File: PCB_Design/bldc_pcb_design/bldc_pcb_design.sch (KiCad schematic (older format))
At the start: 69 parts, among them IC1 DRV8305NPHPR, J1 Conn_01x04_Female, SW1 BOOT, SW2 RESET, U1 ESP32-WROOM-32D, U10 DS18S20Z+, U2 AS5600-ASOT, U3 LM2672M-3.3, U4 CSD18532NQ5B, U5 CSD18532NQ5B, U6 CSD18532NQ5B, U7 CSD18532NQ5B, U8 CSD18532NQ5B, U9 CSD18532NQ5B

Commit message: Routing Iteration 1 done, Rectified schematics (SOx and shunt resistor connections)
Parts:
- removed C2: 68uF 10V, Capacitor_SMD:C_0603_1608Metric, symbol Device:C
- removed C25, C26, C27: 2.2nF, Capacitor_SMD:C_0603_1608Metric, symbol Device:C
- removed C6: 100uF 100V, Capacitor_SMD:C_0603_1608Metric, symbol Device:C
- added C13, C9: 330uF 50V, Capacitor_SMD:CP_Elec_10x10, symbol Device:CP1
- added C15, C18: 10uF 50V, Capacitor_SMD:C_0603_1608Metric, symbol Device:C
- added C2: 68uF 10V, Capacitor_SMD:CP_Elec_6.3x7.7, symbol Device:CP1
- added C6: 100uF 50V, Capacitor_SMD:CP_Elec_6.3x7.7, symbol Device:CP1
- added H3, H4, H6, H7: MountingHole, MountingHole:MountingHole_4mm, symbol Mechanical:MountingHole
- C24: value 1uF 6.3V -> 1uF 6.3V
- R5: value 10k -> 330
- R6: renamed from R11; footprint (none) -> Shunt_Resistor:Shunt_Resistor_L7.0mm_B4.0mm_H1.0mm
- R7: renamed from R13; footprint (none) -> Shunt_Resistor:Shunt_Resistor_L7.0mm_B4.0mm_H1.0mm
- R8: renamed from R14; footprint (none) -> Shunt_Resistor:Shunt_Resistor_L7.0mm_B4.0mm_H1.0mm
- renumbered C8 to C10, C9 to C11, C16 to C12, C17 to C14, C10 to C16, C11 to C17, C12 to C19, C13 to C20, C14 to C21, C19 to C22, C18 to C23, C20 to C25, C28 to C26, C22 to C27, C29 to C28, C23 to C29, C21 to C30, C15 to C8, D4 to D3, D3 to D4, H4 to H1, H5 to H2, H1 to H5, H2 to H8, H3 to H9, R12 to R10, R6 to R11, R7 to R12, R8 to R13, R9 to R14, R10 to R9
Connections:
- net 3V3_IN: now also C2.1
- net GND: now also R6.2, R7.2, R8.2, C13.2, C15.2, C18.2, C2.2, C6.2, C9.2
- net ISENA: now also IC1.16 (SO1); no longer R6.2
- net ISENB: now also IC1.17 (SO2); no longer R7.2
- net ISENC: now also IC1.18 (SO3); no longer R8.2
- net POWER_IN: now also C13.1, C15.1, C18.1, C6.1, C9.1
- net SLA: now also R6.1
- net SLB: now also R7.1
- net SLC: now also R8.1
- removed net SO1: IC1.16 (SO1), R6.1
- removed net SO2: IC1.17 (SO2), R7.1
- removed net SO3: IC1.18 (SO3), R8.1
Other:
- note added: "Current Amplifier Output Pins going to\nADC Pins of ESP32 Microcontroller"
- note added: "LAYOUT GUIDELINES\n1. PWRGD not connected to MCU** (left NC in REV0)\n2. DVDD and AVDD bypass capacitors close to GND\n3. Flying jump caps close to pins\n4. PVDD cap close to PVDD suppply\n5. DRV_WAKE not connected (input from MCU) ** (100ohm to PVDD in REV0)\n6. VDRAIN Should Have Low Impedance Path To Drain Of The High-Side FETs\n7. To include reverse polarity protection ckt at input?** (done i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"
- note added: "Mounting Holes"
- note added: "Note - 68uF not available"
- note added: "Power Connector Pads\n"
- note added: "Power Filter & Decoupling \n Capacitors\n\n"
- note added: "Power Supply (VIN to 3.3V)"
- note removed: "LiPo Battery Connector"
- note removed: "Power Supply (VIN to 3.3v)"
- moved on the sheet: C12, C14, H1, H2, H5, H8, H9, R6, R7, R8

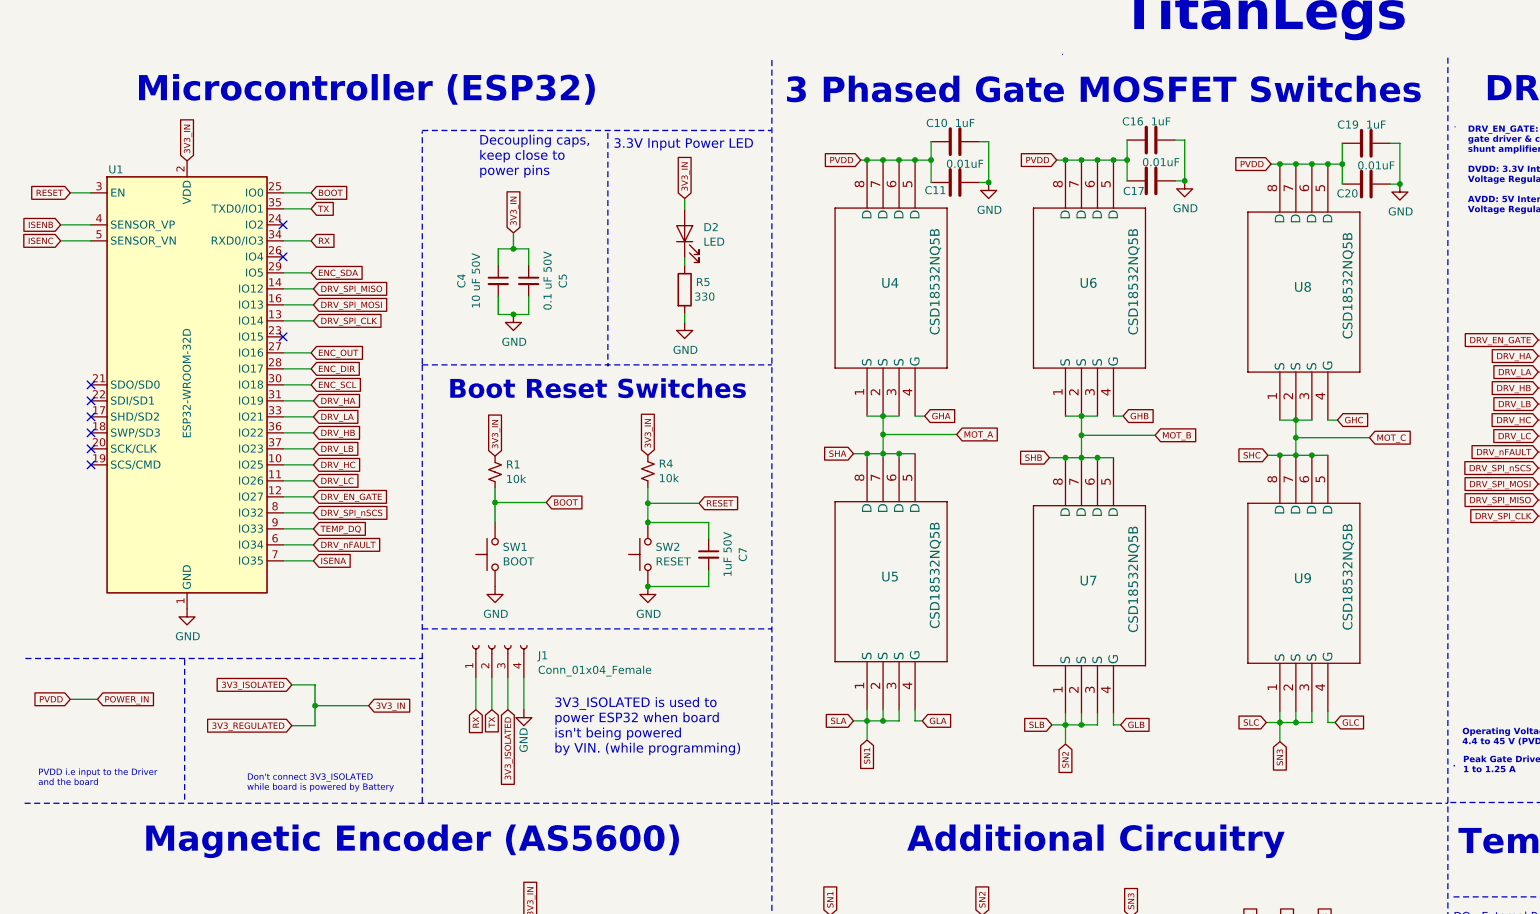
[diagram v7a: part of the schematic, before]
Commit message: Made routing changes and optimized schematics, pcbnew
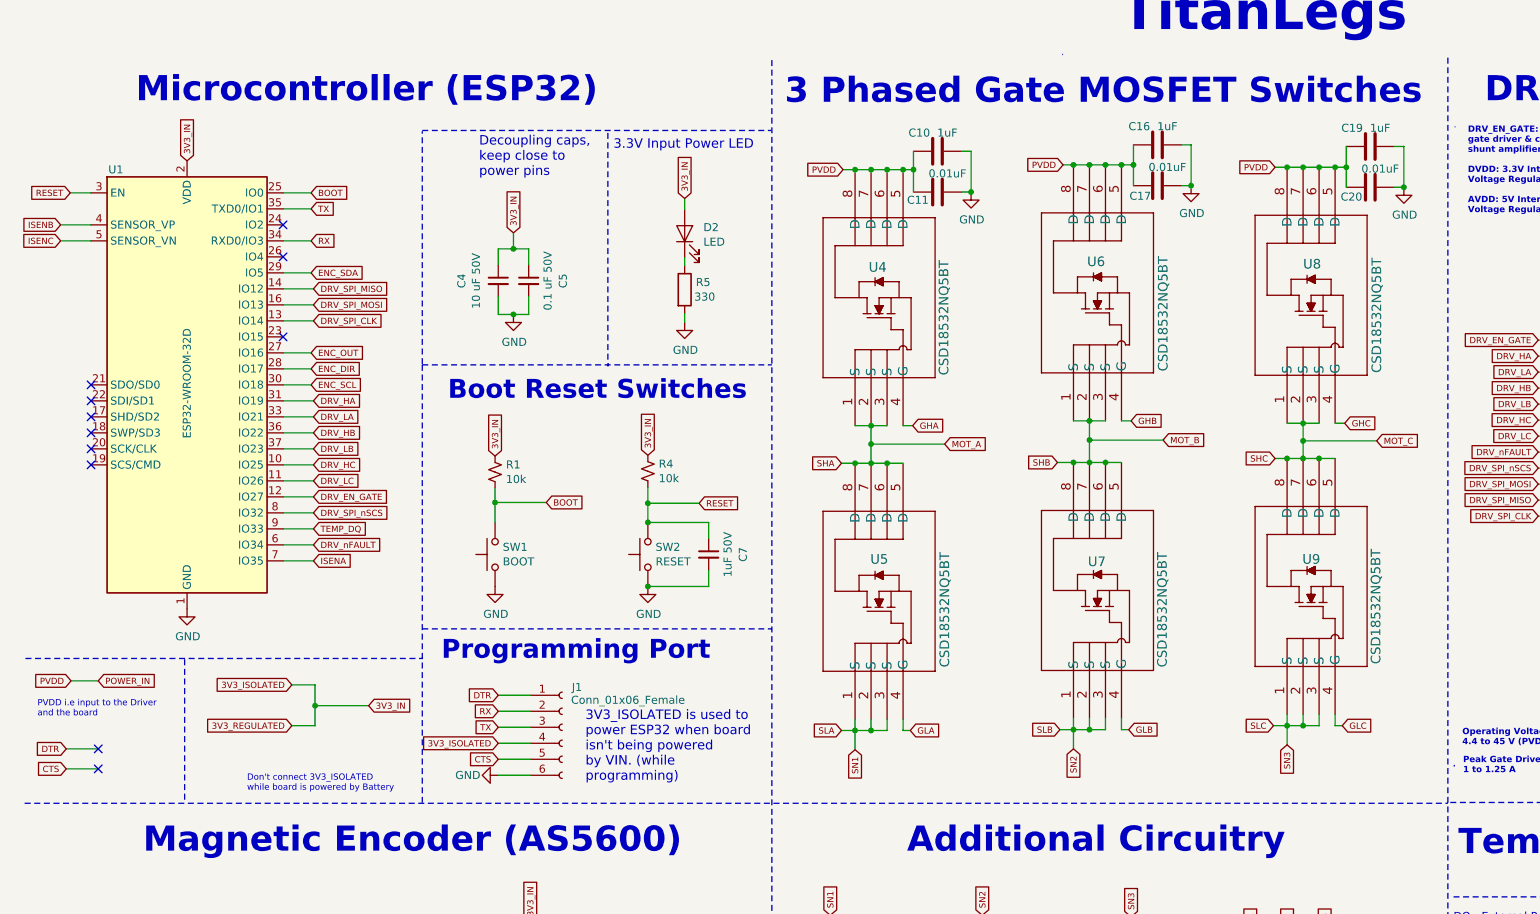
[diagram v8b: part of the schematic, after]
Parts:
- removed J1: Conn_01x04_Female, Connector_PinHeader_2.54mm:PinHeader_1x04_P2.54mm_Vertical, symbol Connector:Conn_01x04_Female
- removed U4, U5, U6, U7, U8, U9: CSD18532NQ5B, CSD18532NQ5B:CSD18532NQ5B, symbol CSD18532NQ5B:CSD18532NQ5B
- added J1: Conn_01x06_Female, Connector_PinHeader_2.54mm:PinHeader_1x06_P2.54mm_Vertical, symbol Connector:Conn_01x06_Female
- added U4, U5, U6, U7, U8, U9: CSD18532NQ5BT, CSD18532NQ5B:CSD18532NQ5B, symbol CSD18532NQ5B:CSD18532NQ5BT
- H1, H2: footprint MountingHole:MountingHole_6mm -> MountingHole:MountingHole_6.4mm_M6_DIN965_Pad
- H5, H8, H9: footprint MountingHole:MountingHole_2.7mm -> MountingHole:MountingHole_2.2mm_M2_DIN965_Pad
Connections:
- net 3V3_IN: now also J1.4 (Pin_4)
- net GHA: now also U4.4 (G)
- net GHB: now also U6.4 (G)
- net GHC: now also U8.4 (G)
- net GLA: now also U5.4 (G)
- net GLB: now also U7.4 (G)
- net GLC: now also U9.4 (G)
- net GND: now also J1.6 (Pin_6)
- net MOT_A: now also U4.1 (S), U4.2 (S), U4.3 (S), U5.5 (D), U5.6 (D), U5.7 (D), U5.8 (D)
- net MOT_B: now also U6.1 (S), U6.2 (S), U6.3 (S), U7.5 (D), U7.6 (D), U7.7 (D), U7.8 (D)
- net MOT_C: now also U8.1 (S), U8.2 (S), U8.3 (S), U9.5 (D), U9.6 (D), U9.7 (D), U9.8 (D)
- net POWER_IN: now also U4.5 (D), U4.6 (D), U4.7 (D), U4.8 (D), U6.5 (D), U6.6 (D), U6.7 (D), U6.8 (D), U8.5 (D), U8.6 (D), U8.7 (D), U8.8 (D)
- net RX: now also J1.2 (Pin_2)
- net SLA: now also U5.1 (S), U5.2 (S), U5.3 (S)
- net SLB: now also U7.1 (S), U7.2 (S), U7.3 (S)
- net SLC: now also U9.1 (S), U9.2 (S), U9.3 (S)
- net TX: now also J1.3 (Pin_3)
- new net CTS: J1.5 (Pin_5)
- new net DTR: J1.1 (Pin_1)
- no-connect marks 14 -> 16
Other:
- note added: "3V3_ISOLATED is used to \npower ESP32 when board \nisn't being powered \nby VIN. (while \nprogramming)\n"
- note added: "Programming Port"
- note removed: "3V3_ISOLATED is used to \npower ESP32 when board \nisn't being powered \nby VIN. (while programming)\n"
- moved on the sheet: C10, C11, C16, C17, C19, C20
